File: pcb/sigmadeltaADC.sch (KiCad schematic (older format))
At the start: 1 part, among them J18 AudioJack3

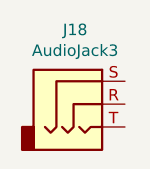
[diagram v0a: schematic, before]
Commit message: Update footprints, move to 0603 passives for JLCPCB assembly, create transformer footprints
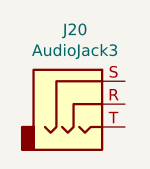
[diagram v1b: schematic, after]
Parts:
- renumbered J18 to J20
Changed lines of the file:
@@
 $EndDescr
 $Comp
-L Connector:AudioJack3 J18
+L Connector:AudioJack3 J20
 U 1 1 60D199BF
 P 1750 2050
-F 0 "J18" H 1732 2375 50  0000 C CNN
+F 0 "J20" H 1732 2375 50  0000 C CNN
 F 1 "AudioJack3" H 1732 2284 50  0000 C CNN
 F 2 "" H 1750 2050 50  0001 C CNN
